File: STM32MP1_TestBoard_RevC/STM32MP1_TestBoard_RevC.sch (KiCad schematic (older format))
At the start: 0 parts

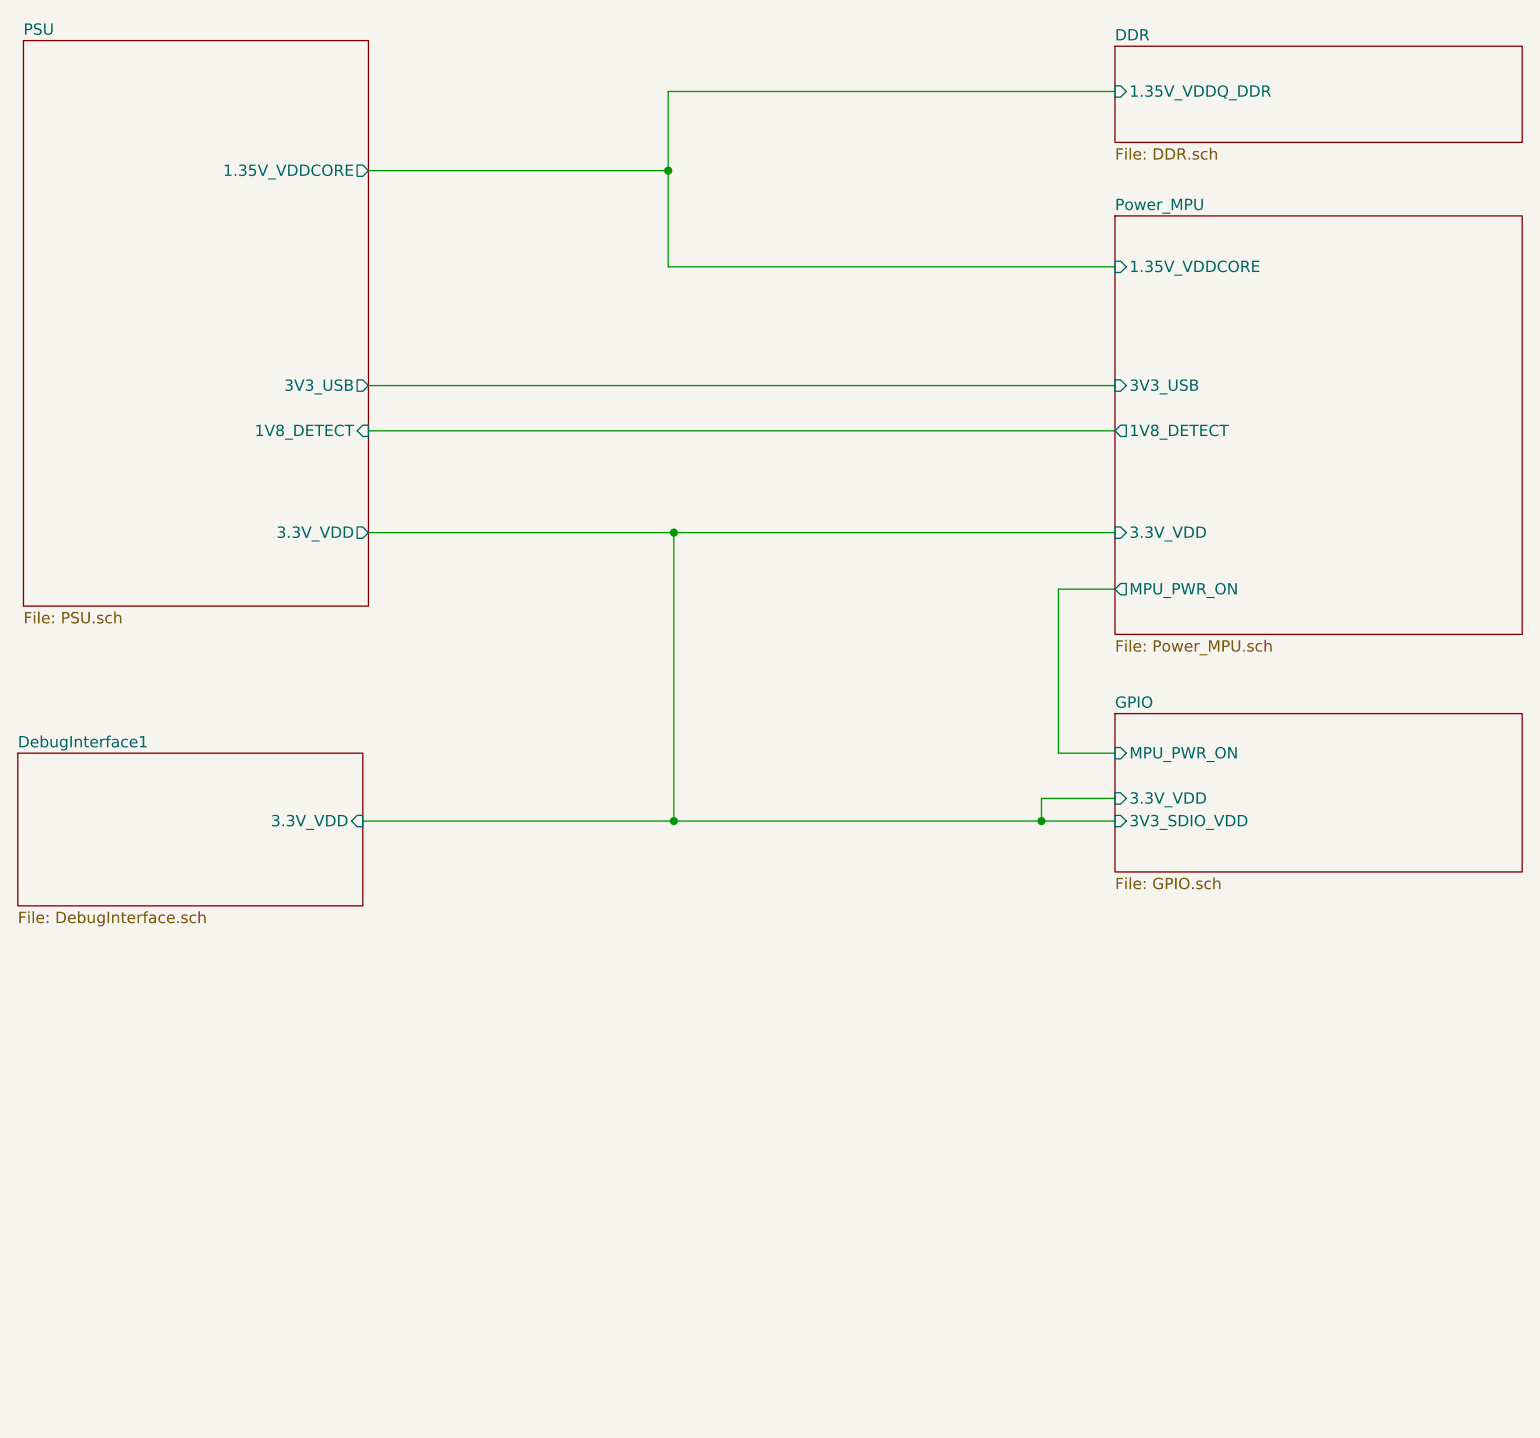
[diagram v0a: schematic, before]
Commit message: HW changes
- Changed buck converter(TPS42402) to LDO (AZ1117)
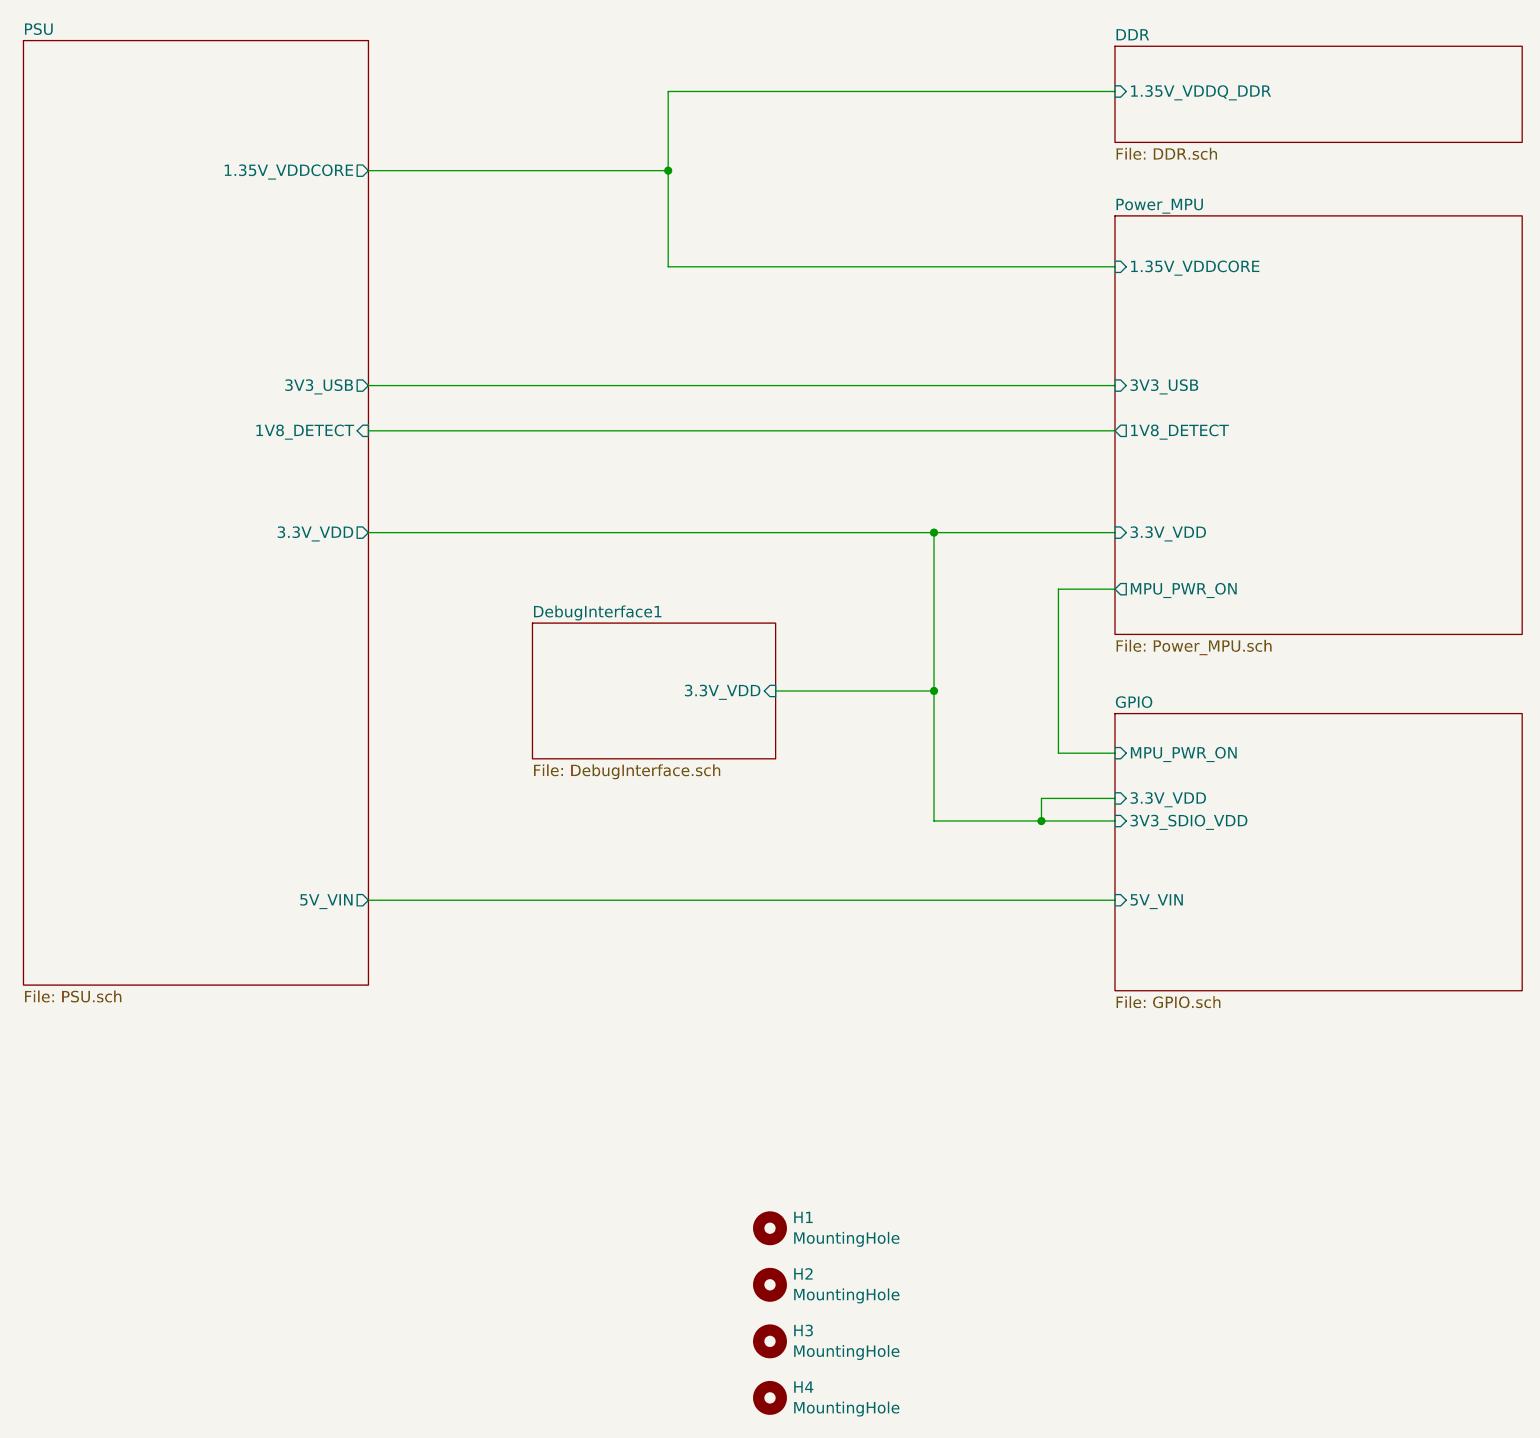
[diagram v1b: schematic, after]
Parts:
- added H1, H2, H3, H4: MountingHole, MountingHole:MountingHole_2.2mm_M2_Pad_Via, symbol Mechanical:MountingHole
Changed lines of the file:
@@
 	6050 5225 9350 5225
 $Sheet
-S 4525 3500 1525 2500
-U 5FBD70AB
-F0 "PSU" 50
-F1 "PSU.sch" 50
-F2 "1V8_DETECT" I R 6050 5225 50
-F3 "1.35V_VDDCORE" O R 6050 4075 50
-F4 "3V3_USB" O R 6050 5025 50
-F5 "3.3V_VDD" O R 6050 5675 50
-$EndSheet
-$Sheet
-S 4500 6650 1525 675
+S 6775 6075 1075 600
 U 606F7DFA
 F0 "DebugInterface1" 50
 F1 "DebugInterface.sch" 50
-F2 "3.3V_VDD" I R 6025 6950 50
+F2 "3.3V_VDD" I R 7850 6375 50
 $EndSheet
 Wire Wire Line
@@
 	6050 4075 7375 4075
 Wire Wire Line
-	9350 5675 7400 5675
+	9350 5675 8550 5675
 Wire Wire Line
 	9350 4500 7375 4500
@@
 	9350 6950 9025 6950
 Wire Wire Line
-	7400 6950 7400 5675
-Connection ~ 7400 5675
+	8550 6950 8550 6375
+Connection ~ 8550 5675
 Wire Wire Line
-	7400 5675 6050 5675
+	8550 5675 6050 5675
 Wire Wire Line
-	6025 6950 7400 6950
-Connection ~ 7400 6950
+	7850 6375 8550 6375
 Wire Wire Line
 	9350 6850 9025 6850
@@
 Connection ~ 9025 6950
 Wire Wire Line
-	9025 6950 7400 6950
+	9025 6950 8550 6950
 Wire Wire Line
 	9350 5025 6050 5025
 $Sheet
-S 9350 6475 1800 700
+S 9350 6475 1800 1225
 U 6097C138
 F0 "GPIO" 50
@@
 F3 "3.3V_VDD" I L 9350 6850 50
 F4 "MPU_PWR_ON" I L 9350 6650 50
+F5 "5V_VIN" I L 9350 7300 50
 $EndSheet
 Wire Wire Line
@@
 Wire Wire Line
 	9100 5925 9350 5925
+$Comp
+L Mechanical:MountingHole H1
+U 1 1 612E02F7
+P 7825 8750
+F 0 "H1" H 7925 8796 50  0000 L CNN
+F 1 "MountingHole" H 7925 8705 50  0000 L CNN
+F 2 "MountingHole:MountingHole_2.2mm_M2_Pad_Via" H 7825 8750 50  0001 C CNN
+F 3 "~" H 7825 8750 50  0001 C CNN
+	1    7825 8750
+	1    0    0    -1
+$EndComp
+$Comp
+L Mechanical:MountingHole H2
+U 1 1 612E1DEF
+P 7825 9000
+F 0 "H2" H 7925 9046 50  0000 L CNN
+F 1 "MountingHole" H 7925 8955 50  0000 L CNN
+F 2 "MountingHole:MountingHole_2.2mm_M2_Pad_Via" H 7825 9000 50  0001 C CNN
+F 3 "~" H 7825 9000 50  0001 C CNN
+	1    7825 9000
+	1    0    0    -1
+$EndComp
+$Comp
+L Mechanical:MountingHole H3
+U 1 1 612E1E5E
+P 7825 9250
+F 0 "H3" H 7925 9296 50  0000 L CNN
+F 1 "MountingHole" H 7925 9205 50  0000 L CNN
+F 2 "MountingHole:MountingHole_2.2mm_M2_Pad_Via" H 7825 9250 50  0001 C CNN
+F 3 "~" H 7825 9250 50  0001 C CNN
+	1    7825 9250
+	1    0    0    -1
+$EndComp
+$Comp
+L Mechanical:MountingHole H4
+U 1 1 612E1ECD
+P 7825 9500
+F 0 "H4" H 7925 9546 50  0000 L CNN
+F 1 "MountingHole" H 7925 9455 50  0000 L CNN
+F 2 "MountingHole:MountingHole_2.2mm_M2_Pad_Via" H 7825 9500 50  0001 C CNN
+F 3 "~" H 7825 9500 50  0001 C CNN
+	1    7825 9500
+	1    0    0    -1
+$EndComp
+$Sheet
+S 4525 3500 1525 4175
+U 5FBD70AB
+F0 "PSU" 50
+F1 "PSU.sch" 50
+F2 "1V8_DETECT" I R 6050 5225 50
+F3 "1.35V_VDDCORE" O R 6050 4075 50
+F4 "3V3_USB" O R 6050 5025 50
+F5 "3.3V_VDD" O R 6050 5675 50
+F6 "5V_VIN" O R 6050 7300 50
+$EndSheet
+Connection ~ 8550 6375
+Wire Wire Line
+	8550 6375 8550 5675
+Wire Wire Line
+	6050 7300 9350 7300
 $EndSCHEMATC
